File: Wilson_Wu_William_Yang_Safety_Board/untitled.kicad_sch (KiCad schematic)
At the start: 24 parts, among them J3 430450200, J5 430450200, J6 XT60-M, J7 XT60-M, Q1 IRLML6344TRPBF, Q2 IRLML6344TRPBF, U16 J115F11AH12VDCS61.5U, U5 J115F11AH12VDCS61.5U, U6 J115F11AH12VDCS61.5U

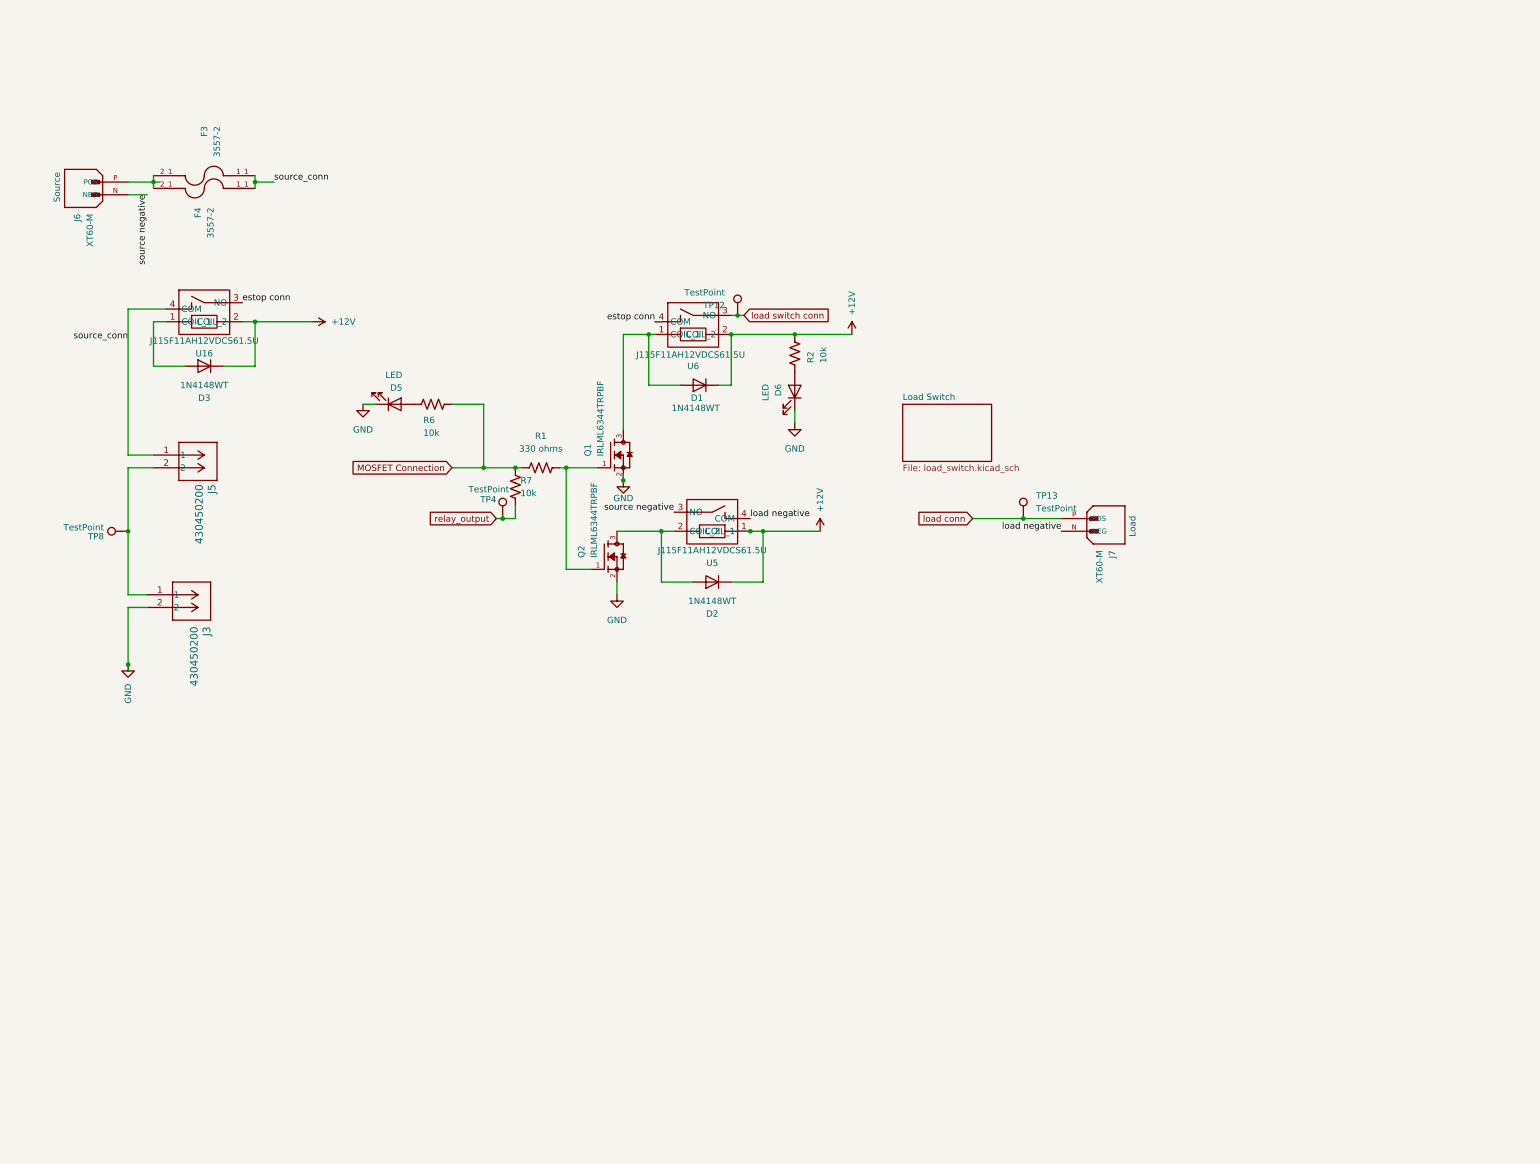
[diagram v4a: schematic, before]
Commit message: changed ldo
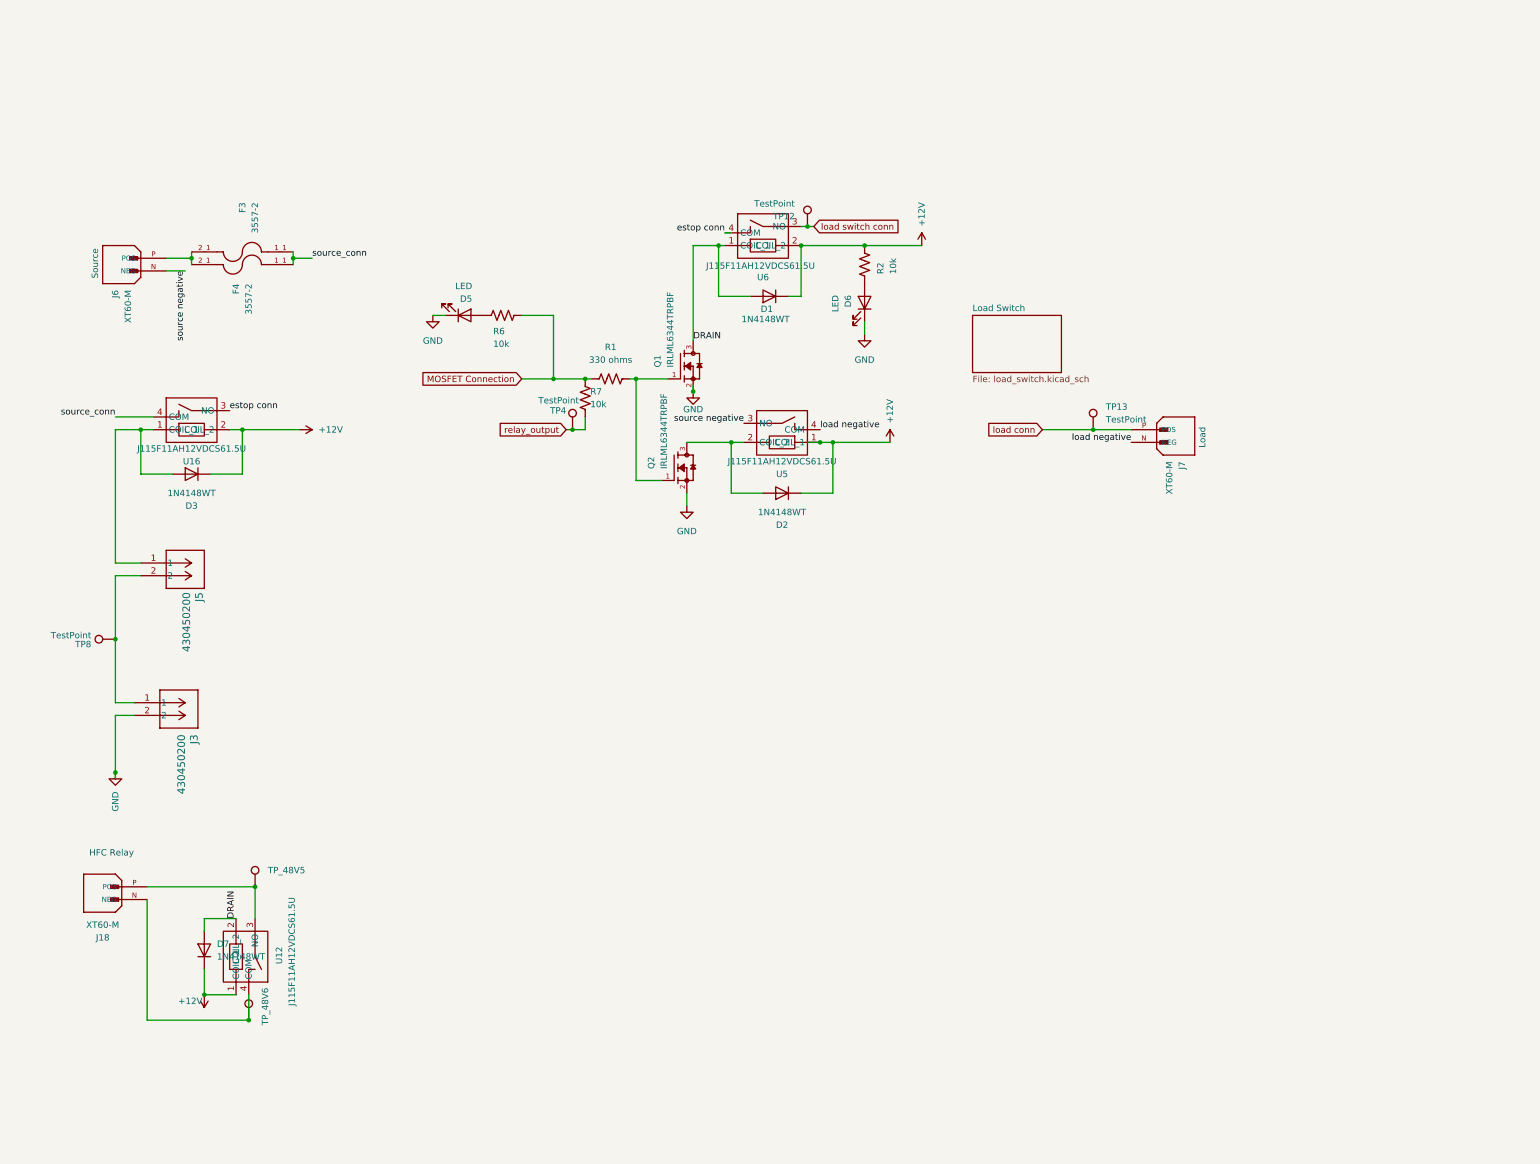
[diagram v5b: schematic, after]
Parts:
- added D7: 1N4148WT, Diode_SMD:D_SOD-523, symbol Diode:1N4148WT
- added J18: XT60-M, SMV_Connectors:AMASS_XT60-M, symbol SMV_Custom:XT60-M
- added TP_48V5, TP_48V6: V_DIVIDED, TestPoint:TestPoint_Pad_D2.0mm, symbol Connector:TestPoint
- added U12: J115F11AH12VDCS61.5U, SMV_Passives:J115F11AH12VDCS615U, symbol SMV_Custom:J115F11AH12VDCS61.5U
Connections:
- net +12V: now also D7.1 (K), U12.1 (COIL_1)
- net source_conn: no longer J5.1
- net DRAIN: now reaches D1.2 (A), Q1.3, U6.1 (COIL_1)
- net DRAIN: now also D7.2 (A), U12.2 (COIL_2)
- net at D3.2 (A), U16.1 (COIL_1): now also J5.1
- new net: J18.N (NEG), TP_48V6.1, U12.4 (COM)
- new net: J18.P (POS), TP_48V5.1, U12.3 (NO)
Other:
- note added: "HFC Relay"
- moved on the sheet: D1, D2, D3, D5, D6, F3, F4, J3, J5, J6, J7, Q1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

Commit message: layout
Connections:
- net load negative: now also U5.3 (NO); no longer U5.4 (COM)
- net source negative: now also U5.4 (COM); no longer U5.3 (NO)
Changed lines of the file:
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@@
+		)
+	)
+	(label "load negative"
+		(at 152.4 67.31 180)
+		(effects
+			(font
+				(size 1.27 1.27)
+			)
+			(justify right bottom)
 		)
 	)
@@
 			)
 			(justify right bottom)
-		)
-	)
-	(label "load negative"
-		(at 167.64 68.58 0)
-		(effects
-			(font
-				(size 1.27 1.27)
-			)
-			(justify left bottom)
 		)
 	)
@@
 	(label "source_conn"
 		(at 26.67 66.04 180)
-		(effects
-			(font
-				(size 1.27 1.27)
-			)
-			(justify right bottom)
-		)
-	)
-	(label "source negative"
-		(at 152.4 67.31 180)
 		(effects
 			(font
@@
 		)
 	)
+	(label "source negative"
+		(at 167.64 68.58 0)
+		(effects
+			(font
+				(size 1.27 1.27)
+			)
+			(justify left bottom)
+		)
+	)

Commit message: comp placement
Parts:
- added R3, R5: 1k, SMV_Passives:0603_resistors, symbol Device:R_US
- added U13: ISOM8110DFGRQ1, octocoupler:DFG0004A_TEX, symbol octocoupler:ISOM8110DFGRQ1
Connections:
- net +12V: now also R3.1
- net GND: now also U13.3 (EM)
- net at D3.2 (A), J5.1, U16.1 (COIL_1): now also U13.2 (CAT)
- new net: R3.2, U13.1 (AN)
- new net +3V3: R5.1
- new net optocoupler-output: R5.2, U13.4 (COL)
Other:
- moved on the sheet: D7, J18, J3, J5, TP8, TP_48V5, TP_48V6, U12

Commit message: bruh
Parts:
- TP12, TP13: footprint TestPoint:TestPoint_Loop_D2.54mm_Drill1.5mm_Beaded -> TestPoint:TestPoint_Pad_D1.0mm
- TP_48V5, TP_48V6: footprint TestPoint:TestPoint_Pad_D2.0mm -> TestPoint:TestPoint_Pad_D1.0mm
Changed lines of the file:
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@@
 			)
 		)
-		(property "Footprint" "TestPoint:TestPoint_Loop_D2.54mm_Drill1.5mm_Beaded"
+		(property "Footprint" "TestPoint:TestPoint_Pad_D1.0mm"
 			(at 170.18 27.94 0)
 			(effects
@@
 			)
 		)
-		(property "Footprint" "TestPoint:TestPoint_Loop_D2.54mm_Drill1.5mm_Beaded"
+		(property "Footprint" "TestPoint:TestPoint_Pad_D1.0mm"
 			(at 227.33 68.58 0)
 			(effects
@@
 			)
 		)
-		(property "Footprint" "TestPoint:TestPoint_Pad_D2.0mm"
+		(property "Footprint" "TestPoint:TestPoint_Pad_D1.0mm"
 			(at 168.91 105.41 0)
 			(effects
@@
 			)
 		)
-		(property "Footprint" "TestPoint:TestPoint_Pad_D2.0mm"
+		(property "Footprint" "TestPoint:TestPoint_Pad_D1.0mm"
 			(at 167.64 132.08 0)
 			(effects
